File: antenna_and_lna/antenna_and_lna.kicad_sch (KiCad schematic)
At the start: 1 part

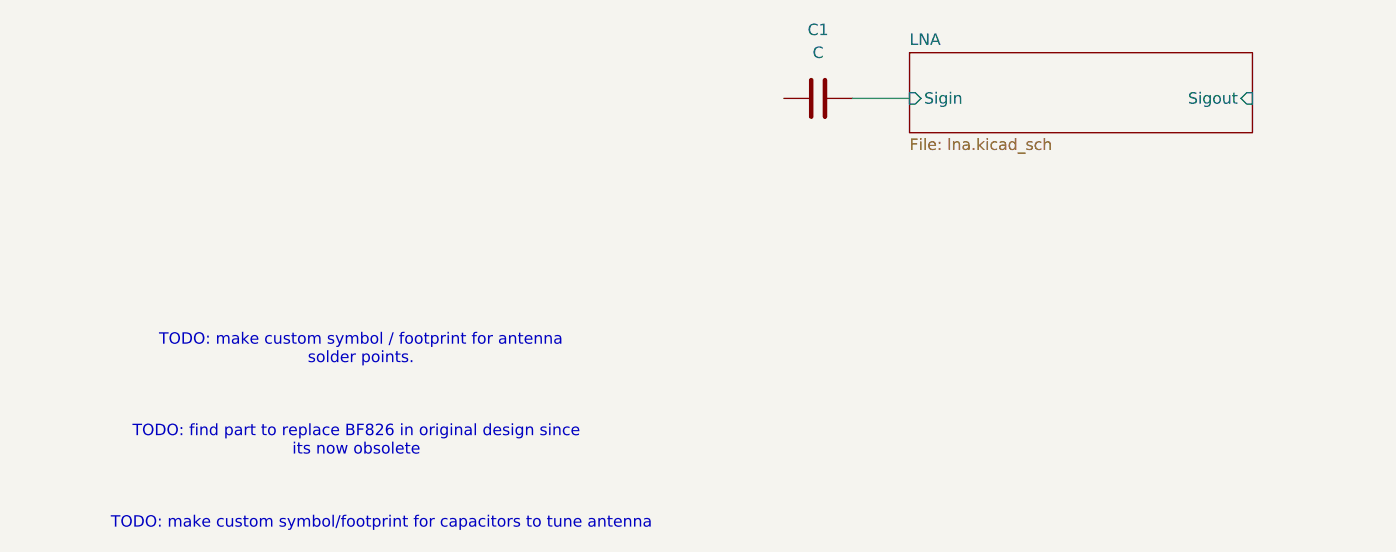
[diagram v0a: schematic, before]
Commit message: update component values for LNA
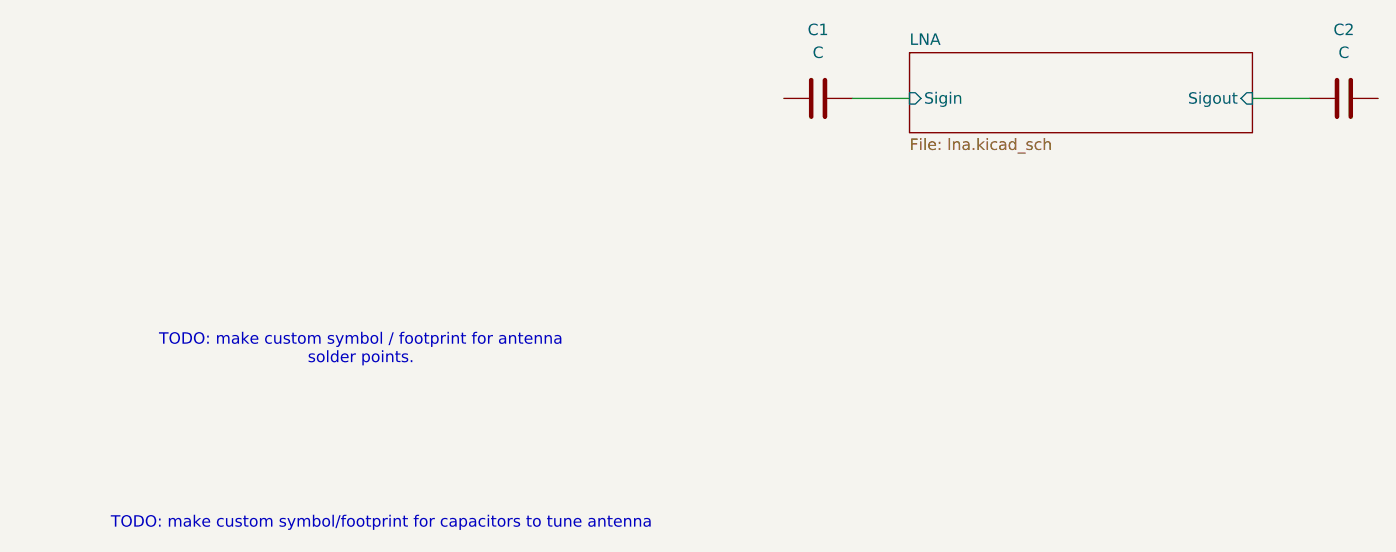
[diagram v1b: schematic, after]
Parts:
- added C2: C, symbol Device:C
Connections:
- net LNA/Sigout: now also C2.1
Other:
- note removed: "TODO: find part to replace BF826 in original design since its now obsolete"
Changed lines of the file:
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@@
 	(generator_version "9.0")
 	(paper "A4")
-	(text "TODO: find part to replace BF826 in original design since \nits now obsolete"
-		(exclude_from_sim no)
-		(at 69.342 134.62 0)
-		(effects
-			(font
-				(size 1.27 1.27)
-			)
-		)
-	)
 	(text "TODO: make custom symbol/footprint for capacitors to tune antenna"
 		(exclude_from_sim no)
@@
 	(wire
 		(pts
+			(xy 168.91 96.52) (xy 175.26 96.52)
+		)
+		(stroke
+			(width 0)
+			(type default)
+		)
+	)
+	(wire
+		(pts
 			(xy 124.46 96.52) (xy 130.81 96.52)
 		)
@@
 		)
 	)
+	(symbol
+		(lib_id "Device:C")
+		(at 179.07 96.52 90)
+		(unit 1)
+		(exclude_from_sim no)
+		(in_bom yes)
+		(on_board yes)
+		(dnp no)
+		(fields_autoplaced yes)
+		(property "Reference" "C2"
+			(at 179.07 88.9 90)
+			(effects
+				(font
+					(size 1.27 1.27)
+				)
+			)
+		)
+		(property "Value" "C"
+			(at 179.07 91.44 90)
+			(effects
+				(font
+					(size 1.27 1.27)
+				)
+			)
+		)
+		(property "Footprint" ""
+			(at 182.88 95.5548 0)
+			(effects
+				(font
+					(size 1.27 1.27)
+				)
+				(hide yes)
+			)
+		)
+		(property "Datasheet" "~"
+			(at 179.07 96.52 0)
+			(effects
+				(font
+					(size 1.27 1.27)
+				)
+				(hide yes)
+			)
+		)
+		(property "Description" "Unpolarized capacitor"
+			(at 179.07 96.52 0)
+			(effects
+				(font
+					(size 1.27 1.27)
+				)
+				(hide yes)
+			)
+		)
+		(pin "2"
+		)
+		(pin "1"
+		)
+		(instances
+			(project ""
+				(path "/c07072f1-c9e3-48f9-9b82-810fab6a13ee"
+					(reference "C2")
+					(unit 1)
+				)
+			)
+		)
+	)

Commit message: add footprints, place parts on board
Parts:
- C1, C2: footprint (none) -> Capacitor_SMD:C_0201_0603Metric
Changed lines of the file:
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@@
 			)
 		)
-		(property "Footprint" ""
+		(property "Footprint" "Capacitor_SMD:C_0201_0603Metric"
 			(at 182.88 95.5548 0)
 			(effects
@@
 			)
 		)
-		(property "Footprint" ""
+		(property "Footprint" "Capacitor_SMD:C_0201_0603Metric"
 			(at 124.46 95.5548 0)
 			(effects

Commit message: add todo message about footprints
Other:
- note added: "TODO: are 0603 footprints good for resistors??"
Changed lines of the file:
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@@
 	(generator_version "9.0")
 	(paper "A4")
+	(text "TODO: are 0603 footprints good for resistors??"
+		(exclude_from_sim no)
+		(at 60.452 160.528 0)
+		(effects
+			(font
+				(size 1.27 1.27)
+			)
+		)
+	)
 	(text "TODO: make custom symbol/footprint for capacitors to tune antenna"
 		(exclude_from_sim no)

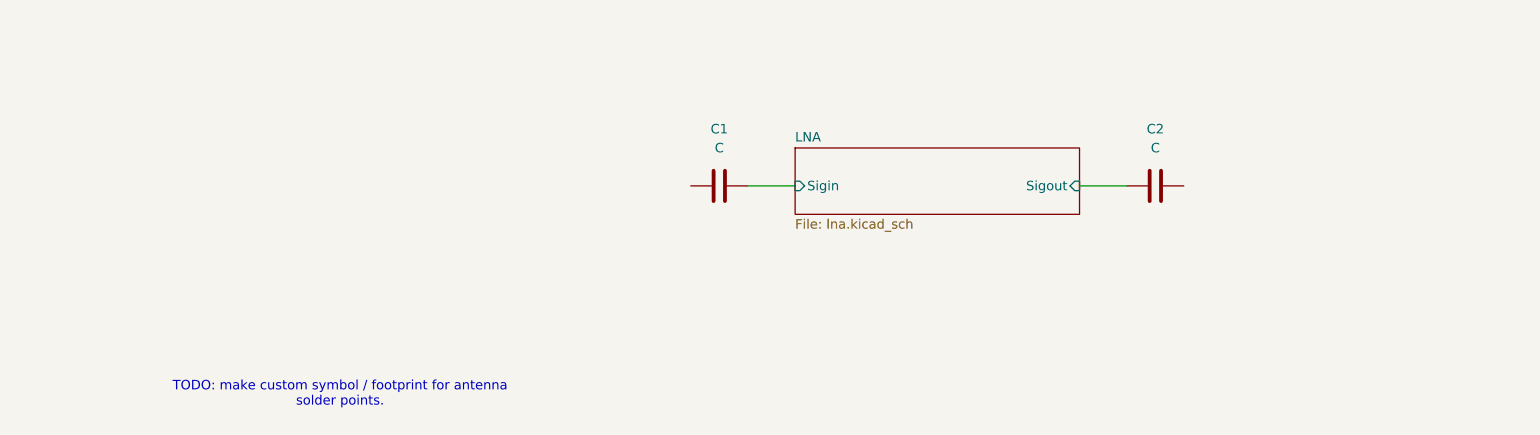
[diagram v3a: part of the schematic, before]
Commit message: add really rough and imprecise (not to scale at all!) footprints for antenna and tuning cap array
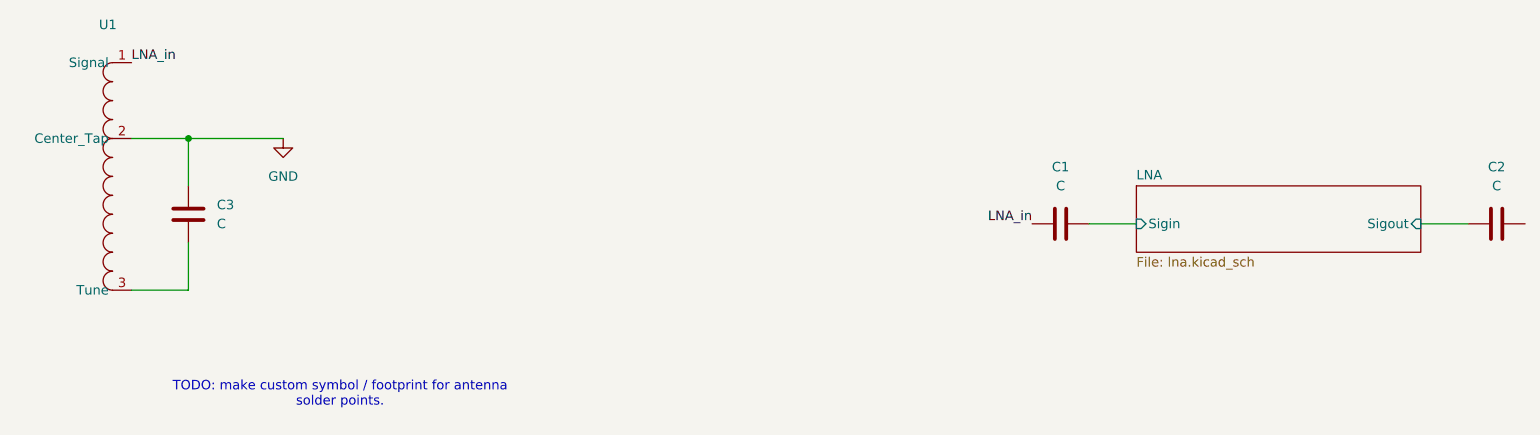
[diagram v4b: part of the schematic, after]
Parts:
- added C3: C, custom:Tuning_Cap, symbol Device:C
- added U1: ~, custom:Antenna, symbol custom:Antenna
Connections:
- net LNA_in: now reaches C1.1
- net LNA_in: now also U1.1 (Signal)
- new net: C3.2, U1.3 (Tune)
- new net GND: C3.1, U1.2 (Center_Tap)
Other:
- moved on the sheet: C1, C2

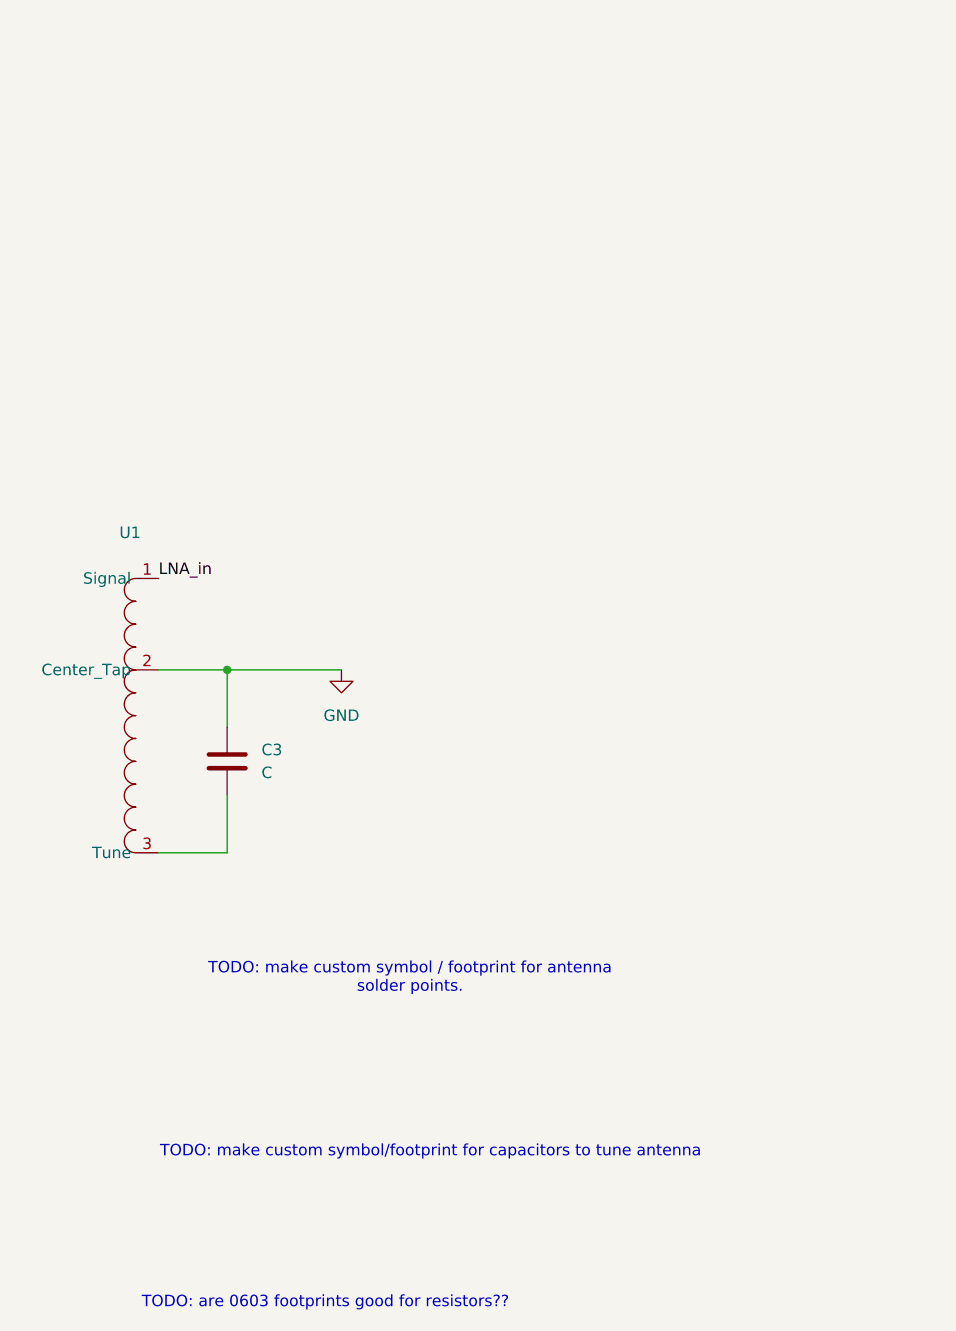
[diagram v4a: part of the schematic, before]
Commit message: add decoupling caps on antenna board
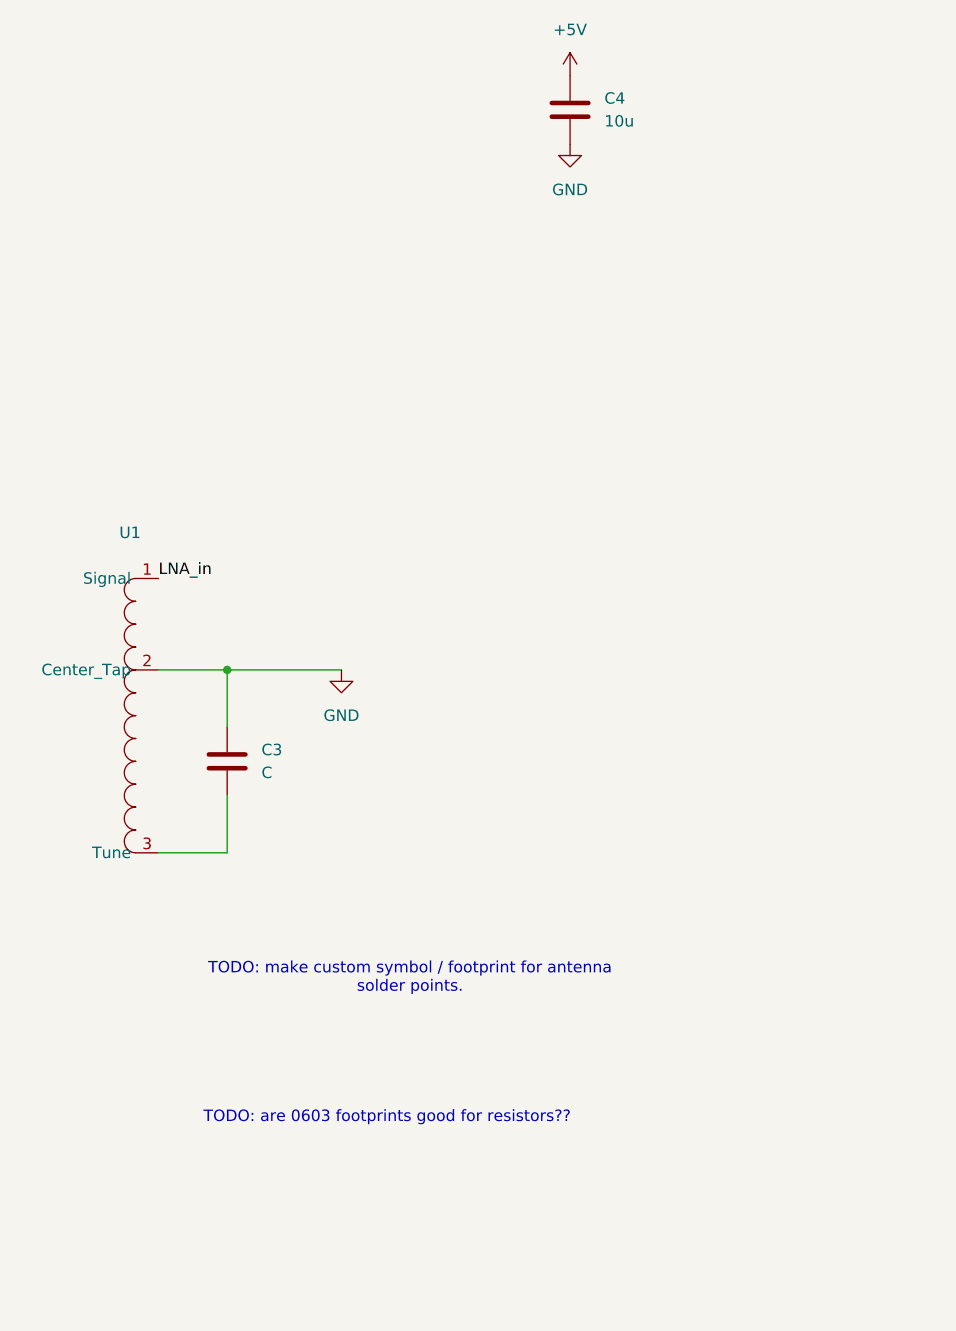
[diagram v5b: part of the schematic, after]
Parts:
- added C4: 10u, symbol Device:C
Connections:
- net GND: now also C4.2
- new net +5V: C4.1
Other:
- note removed: "TODO: make custom symbol/footprint for capacitors to tune antenna"
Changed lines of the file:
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@@
 	(text "TODO: are 0603 footprints good for resistors??"
 		(exclude_from_sim no)
-		(at 60.452 160.528 0)
-		(effects
-			(font
-				(size 1.27 1.27)
-			)
-		)
-	)
-	(text "TODO: make custom symbol/footprint for capacitors to tune antenna"
-		(exclude_from_sim no)
-		(at 72.136 143.764 0)
+		(at 67.31 139.954 0)
 		(effects
 			(font
@@
 			)
 			(justify left bottom)
+		)
+	)
+	(symbol
+		(lib_id "power:+5V")
+		(at 87.63 24.13 0)
+		(unit 1)
+		(exclude_from_sim no)
+		(in_bom yes)
+		(on_board yes)
+		(dnp no)
+		(fields_autoplaced yes)
+		(property "Reference" "#PWR07"
+			(at 87.63 27.94 0)
+			(effects
+				(font
+					(size 1.27 1.27)
+				)
+				(hide yes)
+			)
+		)
+		(property "Value" "+5V"
+			(at 87.63 19.05 0)
+			(effects
+				(font
+					(size 1.27 1.27)
+				)
+			)
+		)
+		(property "Footprint" ""
+			(at 87.63 24.13 0)
+			(effects
+				(font
+					(size 1.27 1.27)
+				)
+				(hide yes)
+			)
+		)
+		(property "Datasheet" ""
+			(at 87.63 24.13 0)
+			(effects
+				(font
+					(size 1.27 1.27)
+				)
+				(hide yes)
+			)
+		)
+		(property "Description" "Power symbol creates a global label with name \"+5V\""
+			(at 87.63 24.13 0)
+			(effects
+				(font
+					(size 1.27 1.27)
+				)
+				(hide yes)
+			)
+		)
+		(pin "1"
+		)
+		(instances
+			(project ""
+				(path "/c07072f1-c9e3-48f9-9b82-810fab6a13ee"
+					(reference "#PWR07")
+					(unit 1)
+				)
+			)
+		)
+	)
+	(symbol
+		(lib_id "power:GND")
+		(at 87.63 31.75 0)
+		(unit 1)
+		(exclude_from_sim no)
+		(in_bom yes)
+		(on_board yes)
+		(dnp no)
+		(fields_autoplaced yes)
+		(property "Reference" "#PWR06"
+			(at 87.63 38.1 0)
+			(effects
+				(font
+					(size 1.27 1.27)
+				)
+				(hide yes)
+			)
+		)
+		(property "Value" "GND"
+			(at 87.63 36.83 0)
+			(effects
+				(font
+					(size 1.27 1.27)
+				)
+			)
+		)
+		(property "Footprint" ""
+			(at 87.63 31.75 0)
+			(effects
+				(font
+					(size 1.27 1.27)
+				)
+				(hide yes)
+			)
+		)
+		(property "Datasheet" ""
+			(at 87.63 31.75 0)
+			(effects
+				(font
+					(size 1.27 1.27)
+				)
+				(hide yes)
+			)
+		)
+		(property "Description" "Power symbol creates a global label with name \"GND\" , ground"
+			(at 87.63 31.75 0)
+			(effects
+				(font
+					(size 1.27 1.27)
+				)
+				(hide yes)
+			)
+		)
+		(pin "1"
+		)
+		(instances
+			(project ""
+				(path "/c07072f1-c9e3-48f9-9b82-810fab6a13ee"
+					(reference "#PWR06")
+					(unit 1)
+				)
+			)
 		)
 	)
@@
 					(unit 1)
 				)
+			)
+		)
+	)
+	(symbol
+		(lib_id "Device:C")
+		(at 87.63 27.94 0)
+		(unit 1)
+		(exclude_from_sim no)
+		(in_bom yes)
+		(on_board yes)
+		(dnp no)
+		(fields_autoplaced yes)
+		(property "Reference" "C4"
+			(at 91.44 26.6699 0)
+			(effects
+				(font
+					(size 1.27 1.27)
+				)
+				(justify left)
+			)
+		)
+		(property "Value" "10u"
+			(at 91.44 29.2099 0)
+			(effects
+				(font
+					(size 1.27 1.27)
+				)
+				(justify left)
+			)
+		)
+		(property "Footprint" ""
+			(at 88.5952 31.75 0)
+			(effects
+				(font
+					(size 1.27 1.27)
+				)
+				(hide yes)
+			)
+		)
+		(property "Datasheet" "~"
+			(at 87.63 27.94 0)
+			(effects
+				(font
+					(size 1.27 1.27)
+				)
+				(hide yes)
+			)
+		)
+		(property "Description" "Unpolarized capacitor"
+			(at 87.63 27.94 0)
+			(effects
+				(font
+					(size 1.27 1.27)
+				)
+				(hide yes)
+			)
+		)
+		(pin "2"
+		)
+		(pin "1"
+		)
+		(instances
+			(project ""
+				(path "/c07072f1-c9e3-48f9-9b82-810fab6a13ee"
+					(reference "C4")
+					(unit 1)
+				)

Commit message: main board gerbers and antenna board layout.
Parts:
- added C6: 3.3n, Capacitor_SMD:C_0603_1608Metric, symbol Device:C
- added J1: CON-SMA-EDGE-S, SMA_fp:RFSOLUTIONS_CON-SMA-EDGE-S, symbol SMA:CON-SMA-EDGE-S
- added J2: TSW-104-14-F-S, pin_header_fp:CON4_1X4_TU_TSW, symbol pin_header:TSW-104-14-F-S
- added L1: 27 u, Inductor_SMD:L_0603_1608Metric, symbol Device:L
- C1: value C -> 100n; footprint Capacitor_SMD:C_0201_0603Metric -> Capacitor_SMD:C_0603_1608Metric
- C2: value C -> .012u; footprint Capacitor_SMD:C_0201_0603Metric -> Capacitor_SMD:C_0603_1608Metric
- C4: footprint (none) -> Capacitor_SMD:C_0603_1608Metric
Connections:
- net +5V: now also J2.1, J2.4
- net GND: now also J1.G1, J1.G2, J1.G3, J1.G4, J2.2, J2.3
- net LNA/Sigout: now also C6.2
- net at C2.2: now also L1.1
- new net ant_to_main: C6.1, J1.1, L1.2
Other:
- note added: "C1 coupling capcitor is not calculated, may require tuning"
- note removed: "TODO: are 0603 footprints good for resistors??"
- note removed: "TODO: make custom symbol / footprint for antenna solder points."
